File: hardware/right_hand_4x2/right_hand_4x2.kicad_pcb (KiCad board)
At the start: 2 copper layers, 115 x 49.5 mm, 18 parts, among them SW1 SW_SPST, SW2 SW_SPST, SW3 SW_SPST, SW4 SW_SPST, SW5 SW_SPST, SW6 SW_SPST, SW7 SW_SPST, SW8 SW_SPST, U1 RP2040-ZERO

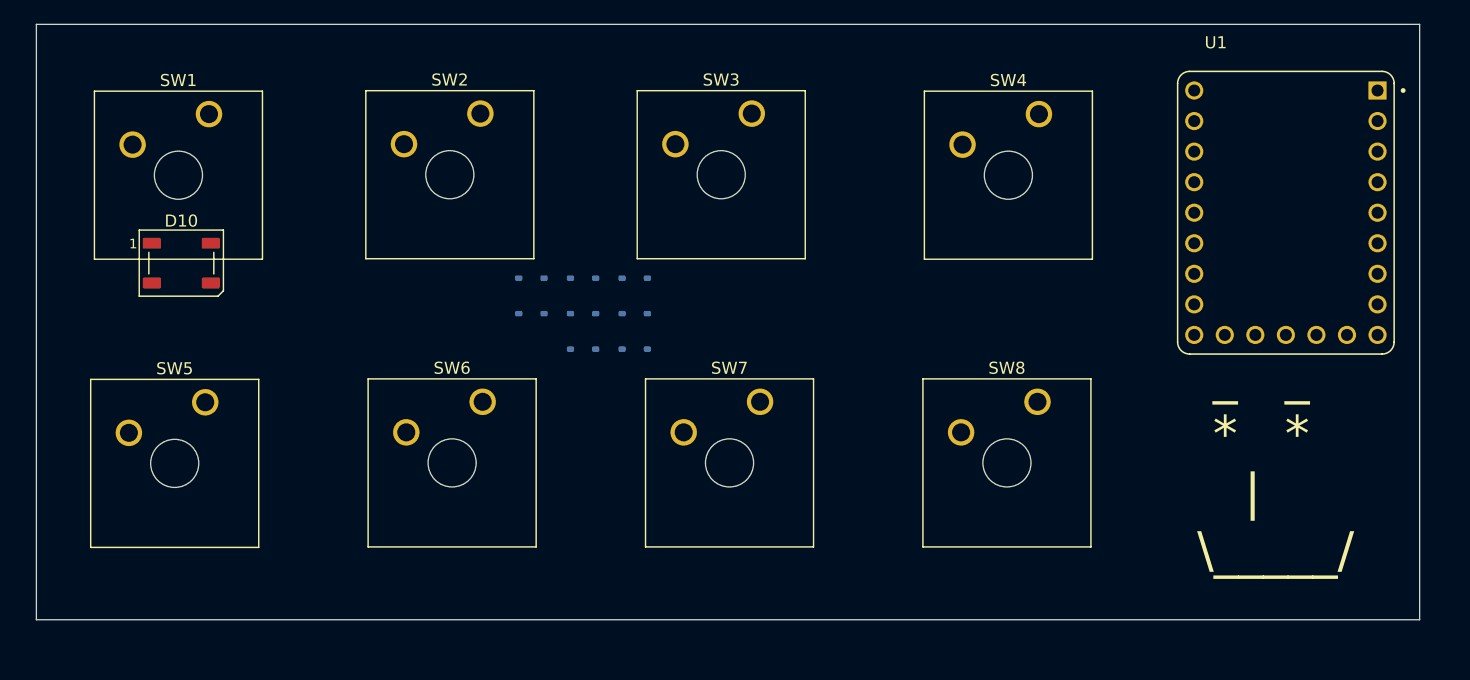
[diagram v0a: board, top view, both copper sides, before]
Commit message: 4x2 schematic and layout update
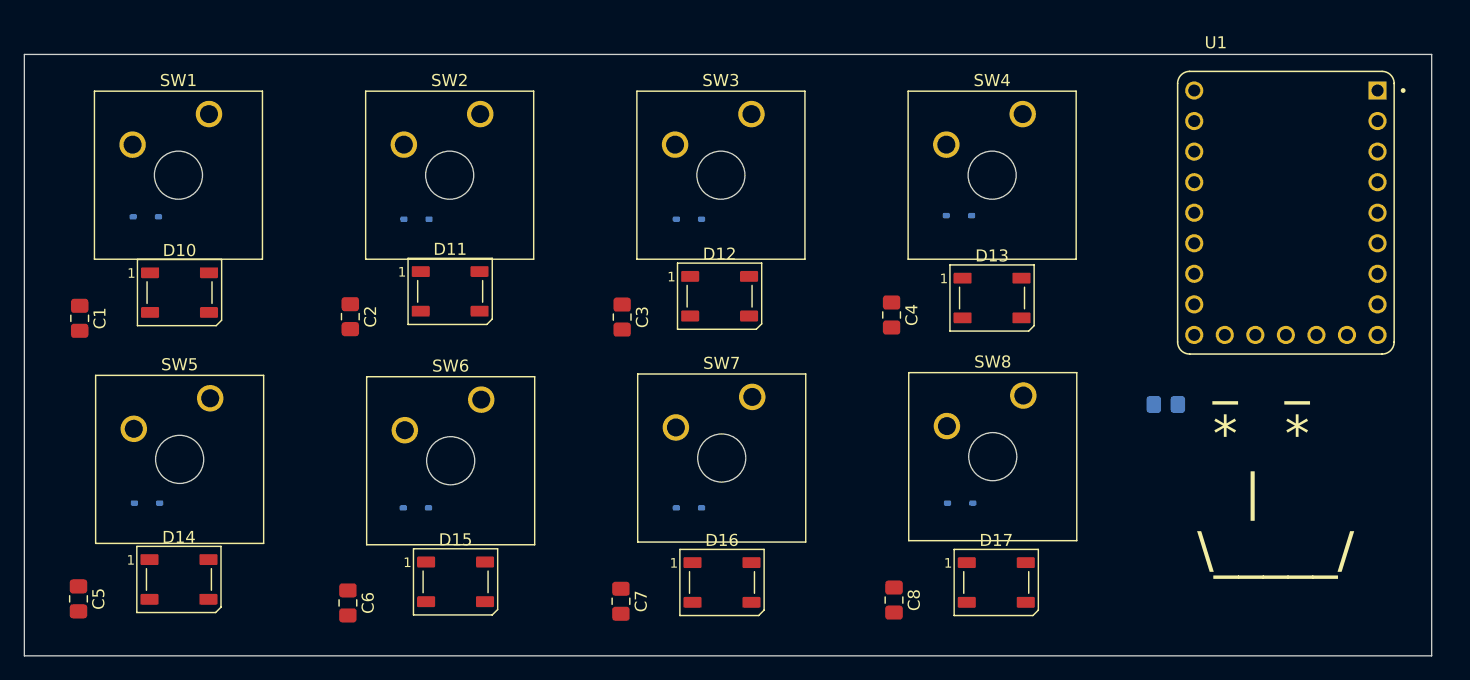
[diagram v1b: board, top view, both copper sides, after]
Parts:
- added C1: C, Capacitor_SMD:C_0805_2012Metric_Pad1.18x1.45mm_HandSolder, F.Cu at (99.6, 66.9)
- added C2: C, Capacitor_SMD:C_0805_2012Metric_Pad1.18x1.45mm_HandSolder, F.Cu at (122.1, 66.8)
- added C3: C, Capacitor_SMD:C_0805_2012Metric_Pad1.18x1.45mm_HandSolder, F.Cu at (144.7, 66.8)
- added C4: C, Capacitor_SMD:C_0805_2012Metric_Pad1.18x1.45mm_HandSolder, F.Cu at (167.1, 66.7)
- added C5: C, Capacitor_SMD:C_0805_2012Metric_Pad1.18x1.45mm_HandSolder, F.Cu at (99.5, 90.3)
- added C6: C, Capacitor_SMD:C_0805_2012Metric_Pad1.18x1.45mm_HandSolder, F.Cu at (121.9, 90.6)
- added C7: C, Capacitor_SMD:C_0805_2012Metric_Pad1.18x1.45mm_HandSolder, F.Cu at (144.6, 90.5)
- added C8: C, Capacitor_SMD:C_0805_2012Metric_Pad1.18x1.45mm_HandSolder, F.Cu at (167.3, 90.4)
- added D11: WS2812B, LED_SMD:LED_WS2812B_PLCC4_5.0x5.0mm_P3.2mm, F.Cu at (130.4, 64.7)
- added D12: WS2812B, LED_SMD:LED_WS2812B_PLCC4_5.0x5.0mm_P3.2mm, F.Cu at (152.8, 65.1)
- added D13: WS2812B, LED_SMD:LED_WS2812B_PLCC4_5.0x5.0mm_P3.2mm, F.Cu at (175.4, 65.2)
- added D14: WS2812B, LED_SMD:LED_WS2812B_PLCC4_5.0x5.0mm_P3.2mm, F.Cu at (107.8, 88.7)
- added D15: WS2812B, LED_SMD:LED_WS2812B_PLCC4_5.0x5.0mm_P3.2mm, F.Cu at (130.8, 88.8)
- added D16: WS2812B, LED_SMD:LED_WS2812B_PLCC4_5.0x5.0mm_P3.2mm, F.Cu at (153.0, 88.9)
- added D17: WS2812B, LED_SMD:LED_WS2812B_PLCC4_5.0x5.0mm_P3.2mm, F.Cu at (175.8, 88.9)
- added R1: R_US, Resistor_SMD:R_0805_2012Metric_Pad1.20x1.40mm_HandSolder, B.Cu at (189.9, 74.1)
- moved D1 41.0 mm to (105.1, 58.5)
- moved D5 39.5 mm to (105.2, 82.3)
- moved D8 39.0 mm to (172.8, 82.3)
- moved D4 31.7 mm to (172.7, 58.4)
- moved D7 23.2 mm to (150.2, 82.7)
- moved D2 19.8 mm to (127.6, 58.7)
- moved D6 19.2 mm to (127.5, 82.7)
- moved D3 11.7 mm to (150.2, 58.7)
- moved D10 2.45 mm to (107.9, 64.8)
- moved SW4 1.35 mm to (178.0, 50.0)
- moved SW8 1.29 mm to (178.1, 73.4)
- moved SW7 0.77 mm to (155.5, 73.5)
- moved SW5 0.53 mm to (110.5, 73.6)
- moved SW6 0.22 mm to (133.0, 73.7)
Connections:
- D10 pad 1: unconnected-(D10-VDD-Pad1) -> +5V
- D10 pad 2: unconnected-(D10-DOUT-Pad2) -> Net-(D10-DOUT)
- D10 pad 3: unconnected-(D10-VSS-Pad3) -> GND
- D10 pad 4: unconnected-(D10-DIN-Pad4) -> rgb
- U1 pad 1: unconnected-(U1-GP0-Pad1) -> col0
- U1 pad 12: unconnected-(U1-GP11-Pad12) -> Net-(U1-GP11)
- U1 pad 2: unconnected-(U1-GP1-Pad2) -> col1
- U1 pad 22: unconnected-(U1-GND-Pad22) -> GND
- U1 pad 23: unconnected-(U1-5V-Pad23) -> +5V
- U1 pad 3: unconnected-(U1-GP2-Pad3) -> col2
- U1 pad 4: unconnected-(U1-GP3-Pad4) -> col3
- U1 pad 6: unconnected-(U1-GP5-Pad6) -> row0
- U1 pad 7: unconnected-(U1-GP6-Pad7) -> row1
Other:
- board size 115 x 49.5 mm -> 117 x 50 mm
